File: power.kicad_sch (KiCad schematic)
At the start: 47 parts, among them CN14 DF40C-30DP-0.4V, CN17 0530470310, J2 TYPE-C16PIN, Q5 CSD17575Q3, Q6 CSD17575Q3, Q7 CSD17575Q3, Q8 CSD17575Q3, U2 CH224K, U3 BQ25792RQMR, U4 AP2112K-3.3TRG1, U5 AP2112K-1.8TRG1, U6 LP8556SQ-E09/NOPB, U9 TPS61088RHLR

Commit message: configured 8-layer pcb with micro vias, finished power mezzanine routing, completed io port, started work on slateconnect mezzanine
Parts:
- L2, L4: footprint (none) -> slate113:IND-SMD_L7.1-W6.5-P5.60
- L3: footprint (none) -> slate113:IND-SMD_L7.1-W6.6
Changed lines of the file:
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@@
 			)
 		)
-		(property "Footprint" ""
+		(property "Footprint" "slate113:IND-SMD_L7.1-W6.5-P5.60"
 			(at 147.32 93.98 0)
 			(hide yes)
@@
 		)
 		(property "LCSC Part" "C87572"
-			(at 147.32 93.98 0) (hide yes) (show_name no) (do_not_autoplace no)
-			(effects (font (size 1.27 1.27)))
+			(at 147.32 93.98 0)
+			(hide yes)
+			(show_name no)
+			(do_not_autoplace no)
+			(effects
+				(font
+					(size 1.27 1.27)
+				)
+			)
 		)
 		(property "MPN" "SPM6530T-1R0M120"
-			(at 147.32 93.98 0) (hide yes) (show_name no) (do_not_autoplace no)
-			(effects (font (size 1.27 1.27)))
+			(at 147.32 93.98 0)
+			(hide yes)
+			(show_name no)
+			(do_not_autoplace no)
+			(effects
+				(font
+					(size 1.27 1.27)
+				)
+			)
 		)
 		(property "Manufacturer" "TDK"
-			(at 147.32 93.98 0) (hide yes) (show_name no) (do_not_autoplace no)
-			(effects (font (size 1.27 1.27)))
+			(at 147.32 93.98 0)
+			(hide yes)
+			(show_name no)
+			(do_not_autoplace no)
+			(effects
+				(font
+					(size 1.27 1.27)
+				)
+			)
 		)
 		(pin "1"
@@
 			)
 		)
-		(property "Footprint" ""
+		(property "Footprint" "slate113:IND-SMD_L7.1-W6.6"
 			(at 96.52 97.79 0)
 			(hide yes)
@@
 		)
 		(property "LCSC Part" "C112288"
-			(at 96.52 97.79 0) (hide yes) (show_name no) (do_not_autoplace no)
-			(effects (font (size 1.27 1.27)))
+			(at 96.52 97.79 0)
+			(hide yes)
+			(show_name no)
+			(do_not_autoplace no)
+			(effects
+				(font
+					(size 1.27 1.27)
+				)
+			)
 		)
 		(property "MPN" "SPM6530T-100M"
-			(at 96.52 97.79 0) (hide yes) (show_name no) (do_not_autoplace no)
-			(effects (font (size 1.27 1.27)))
+			(at 96.52 97.79 0)
+			(hide yes)
+			(show_name no)
+			(do_not_autoplace no)
+			(effects
+				(font
+					(size 1.27 1.27)
+				)
+			)
 		)
 		(property "Manufacturer" "TDK"
-			(at 96.52 97.79 0) (hide yes) (show_name no) (do_not_autoplace no)
-			(effects (font (size 1.27 1.27)))
+			(at 96.52 97.79 0)
+			(hide yes)
+			(show_name no)
+			(do_not_autoplace no)
+			(effects
+				(font
+					(size 1.27 1.27)
+				)
+			)
 		)
 		(pin "1"
@@
 			)
 		)
-		(property "Footprint" ""
+		(property "Footprint" "slate113:IND-SMD_L7.1-W6.5-P5.60"
 			(at 85.09 41.91 0)
 			(hide yes)
@@
 		)
 		(property "LCSC Part" "C87572"
-			(at 85.09 41.91 0) (hide yes) (show_name no) (do_not_autoplace no)
-			(effects (font (size 1.27 1.27)))
+			(at 85.09 41.91 0)
+			(hide yes)
+			(show_name no)
+			(do_not_autoplace no)
+			(effects
+				(font
+					(size 1.27 1.27)
+				)
+			)
 		)
 		(property "MPN" "SPM6530T-1R0M120"
-			(at 85.09 41.91 0) (hide yes) (show_name no) (do_not_autoplace no)
-			(effects (font (size 1.27 1.27)))
+			(at 85.09 41.91 0)
+			(hide yes)
+			(show_name no)
+			(do_not_autoplace no)
+			(effects
+				(font
+					(size 1.27 1.27)
+				)
+			)
 		)
 		(property "Manufacturer" "TDK"
-			(at 85.09 41.91 0) (hide yes) (show_name no) (do_not_autoplace no)
-			(effects (font (size 1.27 1.27)))
+			(at 85.09 41.91 0)
+			(hide yes)
+			(show_name no)
+			(do_not_autoplace no)
+			(effects
+				(font
+					(size 1.27 1.27)
+				)
+			)
 		)
 		(pin "2"

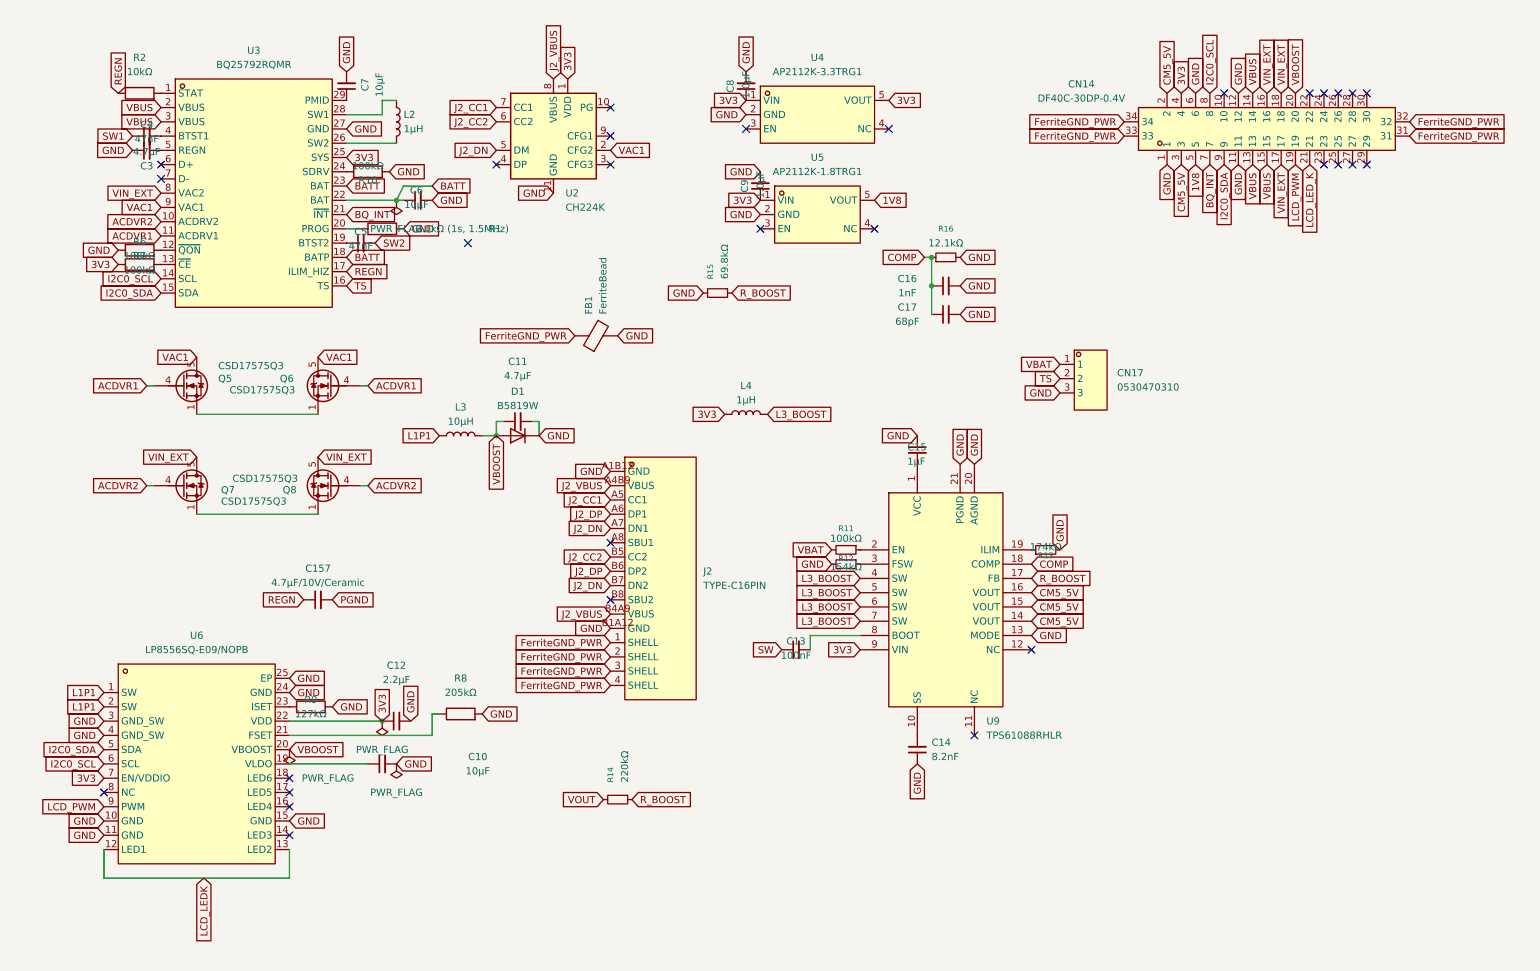
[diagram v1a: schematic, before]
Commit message: finished m.2 board and copper pours, completed antenna bracket and power board, finished slateconnect board, reorganized libraries
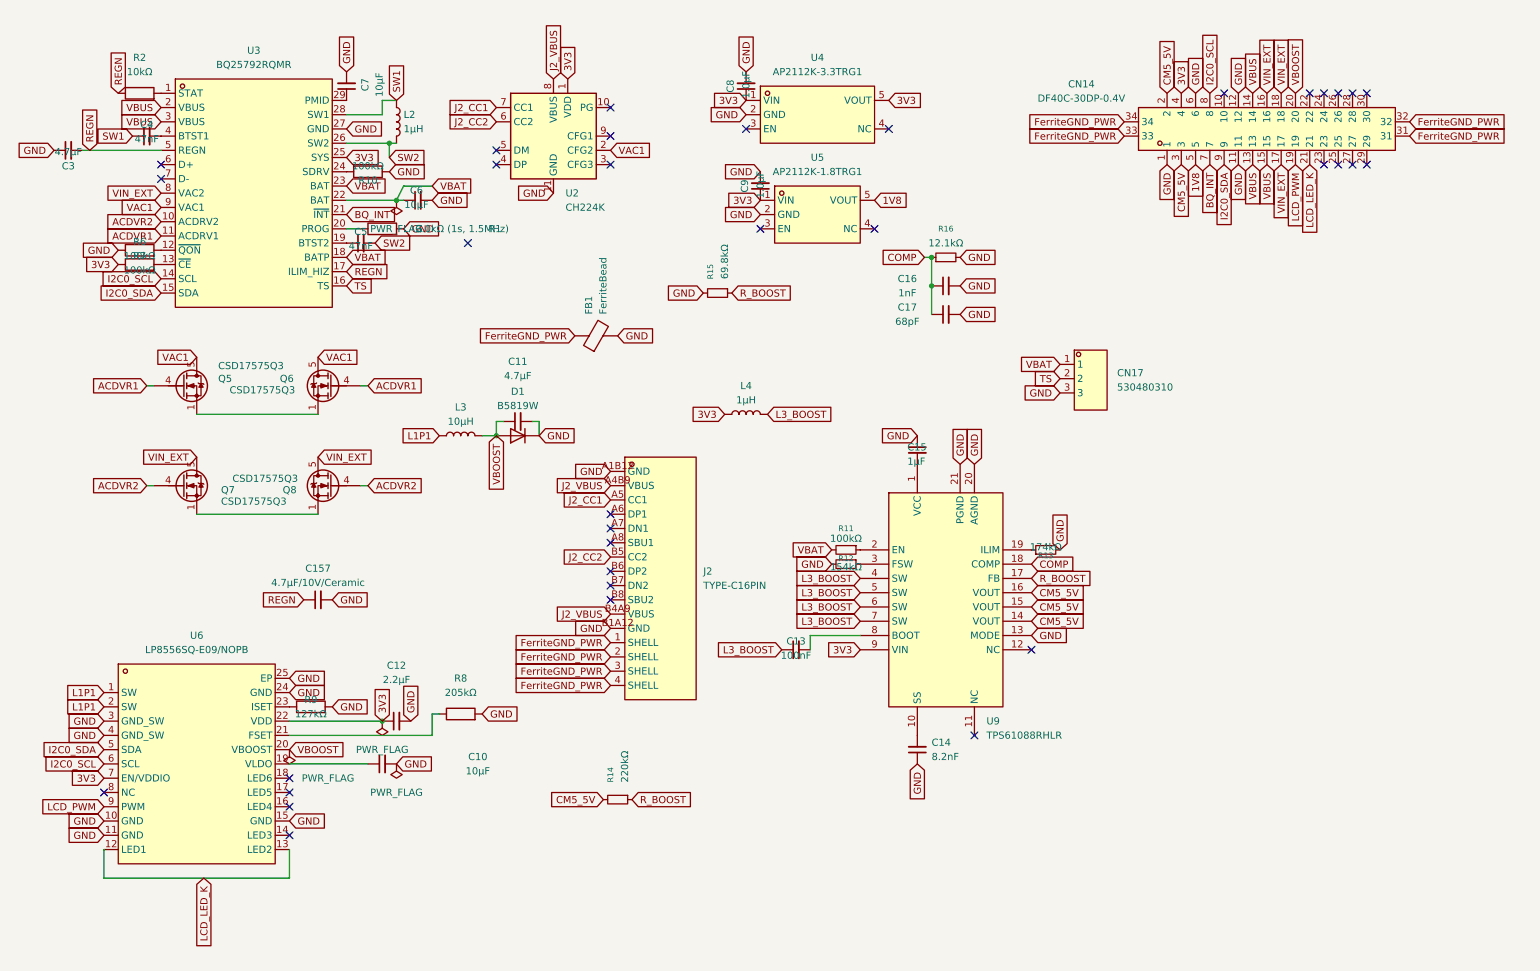
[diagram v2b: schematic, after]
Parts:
- CN17: value 0530470310 -> 530480310; LCSC Part C122442 -> C505275; MPN 0530470310 -> 530480310
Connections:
- net BATT is gone; now on net VBAT: C6.1, U3.18 (BATP), U3.22 (BAT), U3.23 (BAT)
- net LCD_LEDK is gone; now on net LCD_LED_K: U6.12 (LED1), U6.13 (LED2)
- net PGND is gone; now on net GND: C157.2
- net SW is gone; now on net L3_BOOST: C13.1
- net VOUT is gone; now on net CM5_5V: R14.2
- net REGN: now also C3.2, U3.5 (REGN)
- net SW1: now also L2.1, U3.28 (SW1)
- net SW2: now also L2.2, U3.26 (SW2)
- removed net J2_DN: J2.A7 (DN1), J2.B7 (DN2), U2.5 (DM)
- net J2_DP: no longer names the net of J2.A6 (DP1)
- net J2_DP: no longer J2.B6 (DP2)
- no-connect marks 30 -> 35
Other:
- moved on the sheet: C3
